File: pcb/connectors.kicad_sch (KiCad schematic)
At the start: 34 parts, among them J1 Conn_01x02, J4 Conn_01x20, J5 SATA_USB, J6 CPU_USB, SW3 SPVS410100, U5 CH340E, U8 FH35C

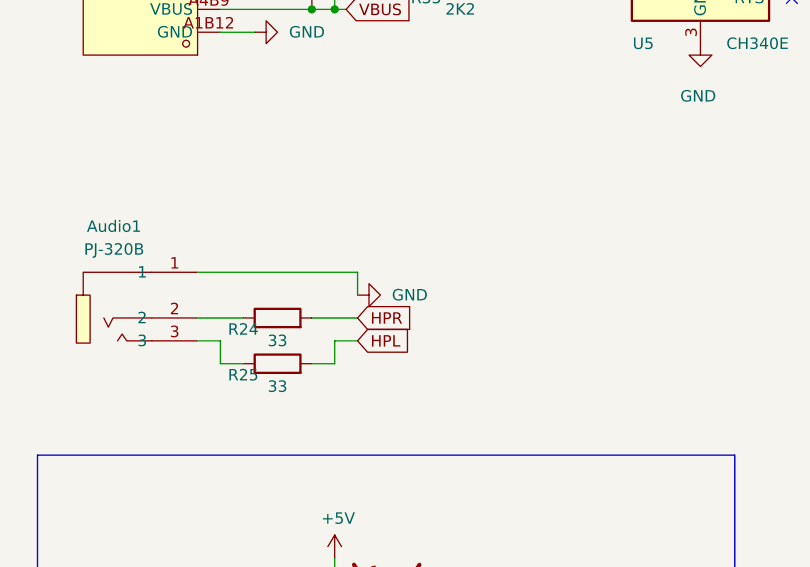
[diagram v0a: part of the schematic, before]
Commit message: Added last minor patches like ideal diode on PCB, added backplate
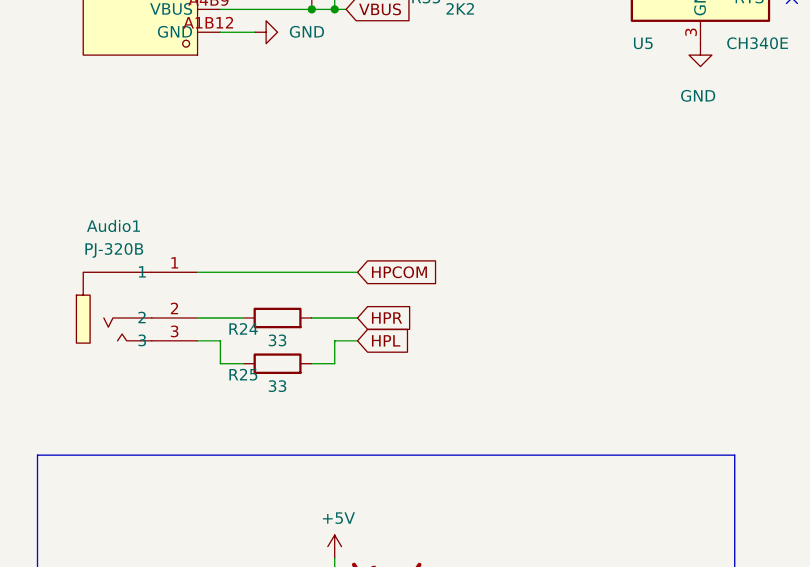
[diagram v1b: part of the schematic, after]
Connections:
- net GND: no longer Audio1.1
- new net HPCOM: Audio1.1
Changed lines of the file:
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@@
+	(wire
+		(pts
+			(xy 31.75 90.17) (xy 49.53 90.17)
+		)
+		(stroke
+			(width 0)
+			(type default)
+		)
+	)
 	(wire
 		(pts
@@
 	(wire
 		(pts
-			(xy 31.75 90.17) (xy 49.53 90.17)
-		)
-		(stroke
-			(width 0)
-			(type default)
-		)
-	)
-	(wire
-		(pts
 			(xy 158.75 123.19) (xy 162.56 123.19)
 		)
@@
 		(pts
 			(xy 207.01 49.53) (xy 190.5 49.53)
-		)
-		(stroke
-			(width 0)
-			(type default)
-		)
-	)
-	(wire
-		(pts
-			(xy 49.53 90.17) (xy 49.53 92.71)
 		)
 		(stroke
@@
 		)
 	)
+	(global_label "HPCOM"
+		(shape input)
+		(at 49.53 90.17 0)
+		(fields_autoplaced yes)
+		(effects
+			(font
+				(size 1.27 1.27)
+			)
+			(justify left)
+		)
+		(property "Intersheetrefs" "${INTERSHEET_REFS}"
+			(at 59.1676 90.17 0)
+			(effects
+				(font
+					(size 1.27 1.27)
+				)
+				(justify left)
+				(hide yes)
+			)
+		)
+	)
 	(global_label "SPI1_CS"
 		(shape input)
@@
 			)
 		)
-	)
-	(symbol
-		(lib_id "power:GND")
-		(at 49.53 92.71 90)
-		(unit 1)
-		(exclude_from_sim no)
-		(in_bom yes)
-		(on_board yes)
-		(dnp no)
-		(property "Reference" "#PWR056"
-			(at 55.88 92.71 0)
-			(effects
-				(font
-					(size 1.27 1.27)
-				)
-				(hide yes)
-			)
-		)
-		(property "Value" "GND"
-			(at 53.34 92.7099 90)
-			(effects
-				(font
-					(size 1.27 1.27)
-				)
-				(justify right)
-			)
-		)
-		(property "Footprint" ""
-			(at 49.53 92.71 0)
-			(effects
-				(font
-					(size 1.27 1.27)
-				)
-				(hide yes)
-			)
-		)
-		(property "Datasheet" ""
-			(at 49.53 92.71 0)
-			(effects
-				(font
-					(size 1.27 1.27)
-				)
-				(hide yes)
-			)
-		)
-		(property "Description" ""
-			(at 49.53 92.71 0)
-			(effects
-				(font
-					(size 1.27 1.27)
-				)
-				(hide yes)
-			)
-		)
-		(pin "1"
-		)
-		(instances
-			(project "minidisc"
-				(path "/521fcede-69d7-4f6d-a594-609fca379ec3/97e92068-8fa4-4c4f-8472-eaf36db290f4"
-					(reference "#PWR056")
-					(unit 1)
-				)
-			)
-		)
